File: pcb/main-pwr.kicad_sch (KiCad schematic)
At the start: 22 parts, among them U2 ADP5054

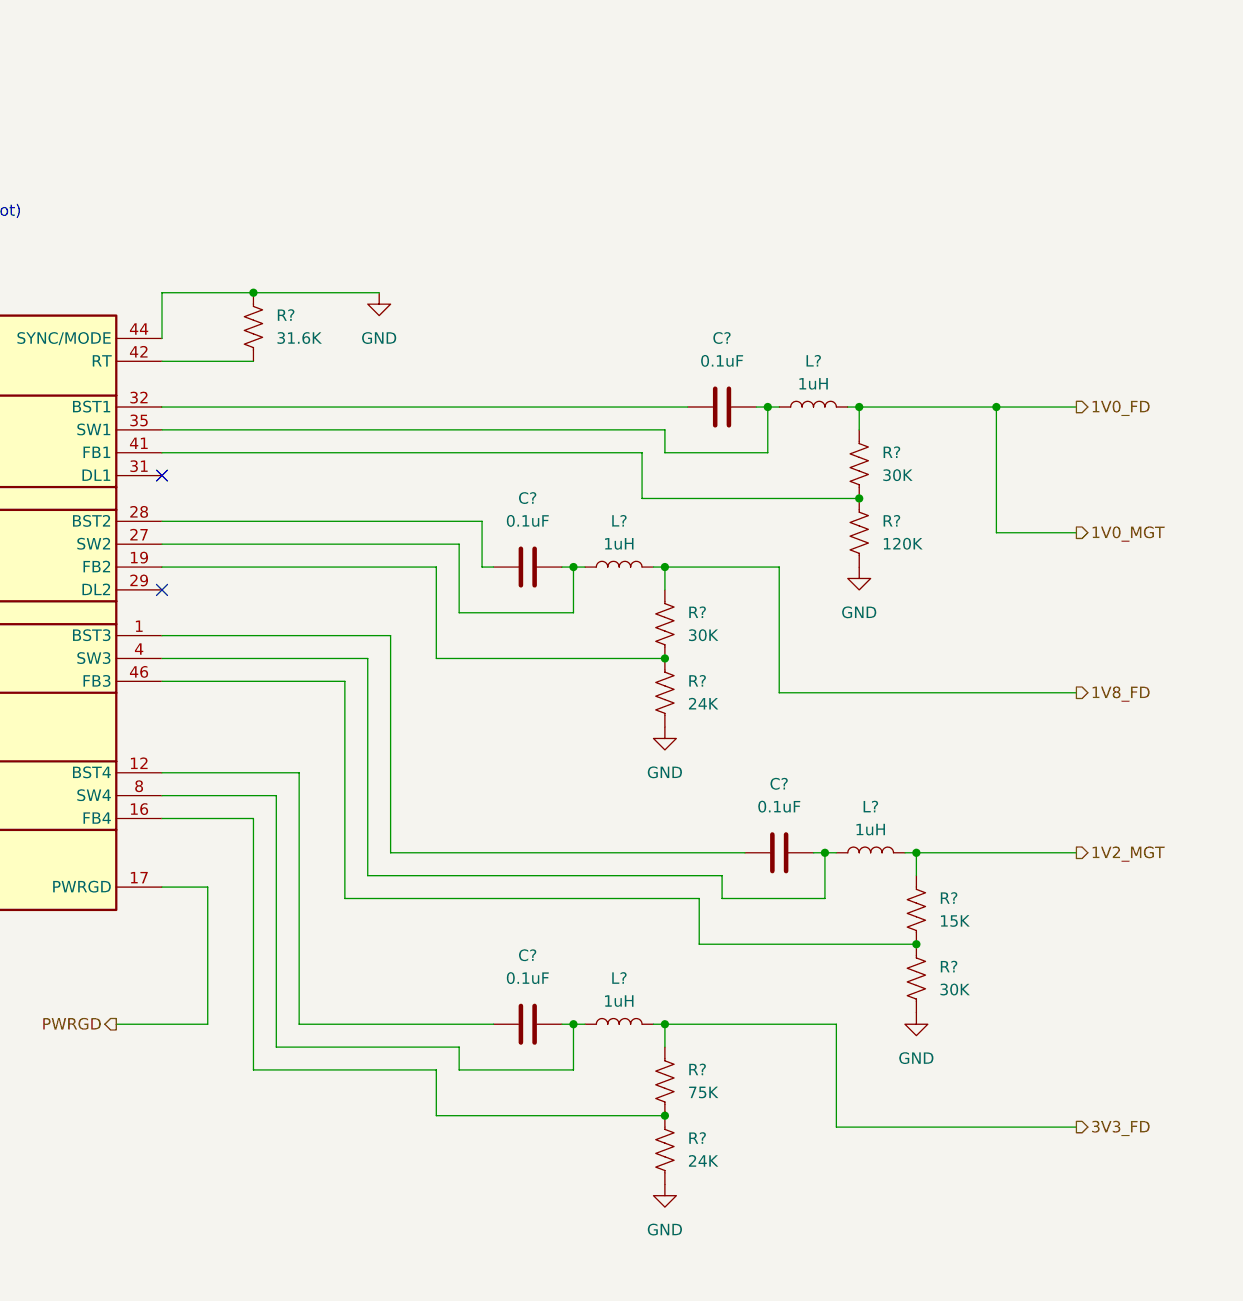
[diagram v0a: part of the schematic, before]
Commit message: current sense hierarchy definition
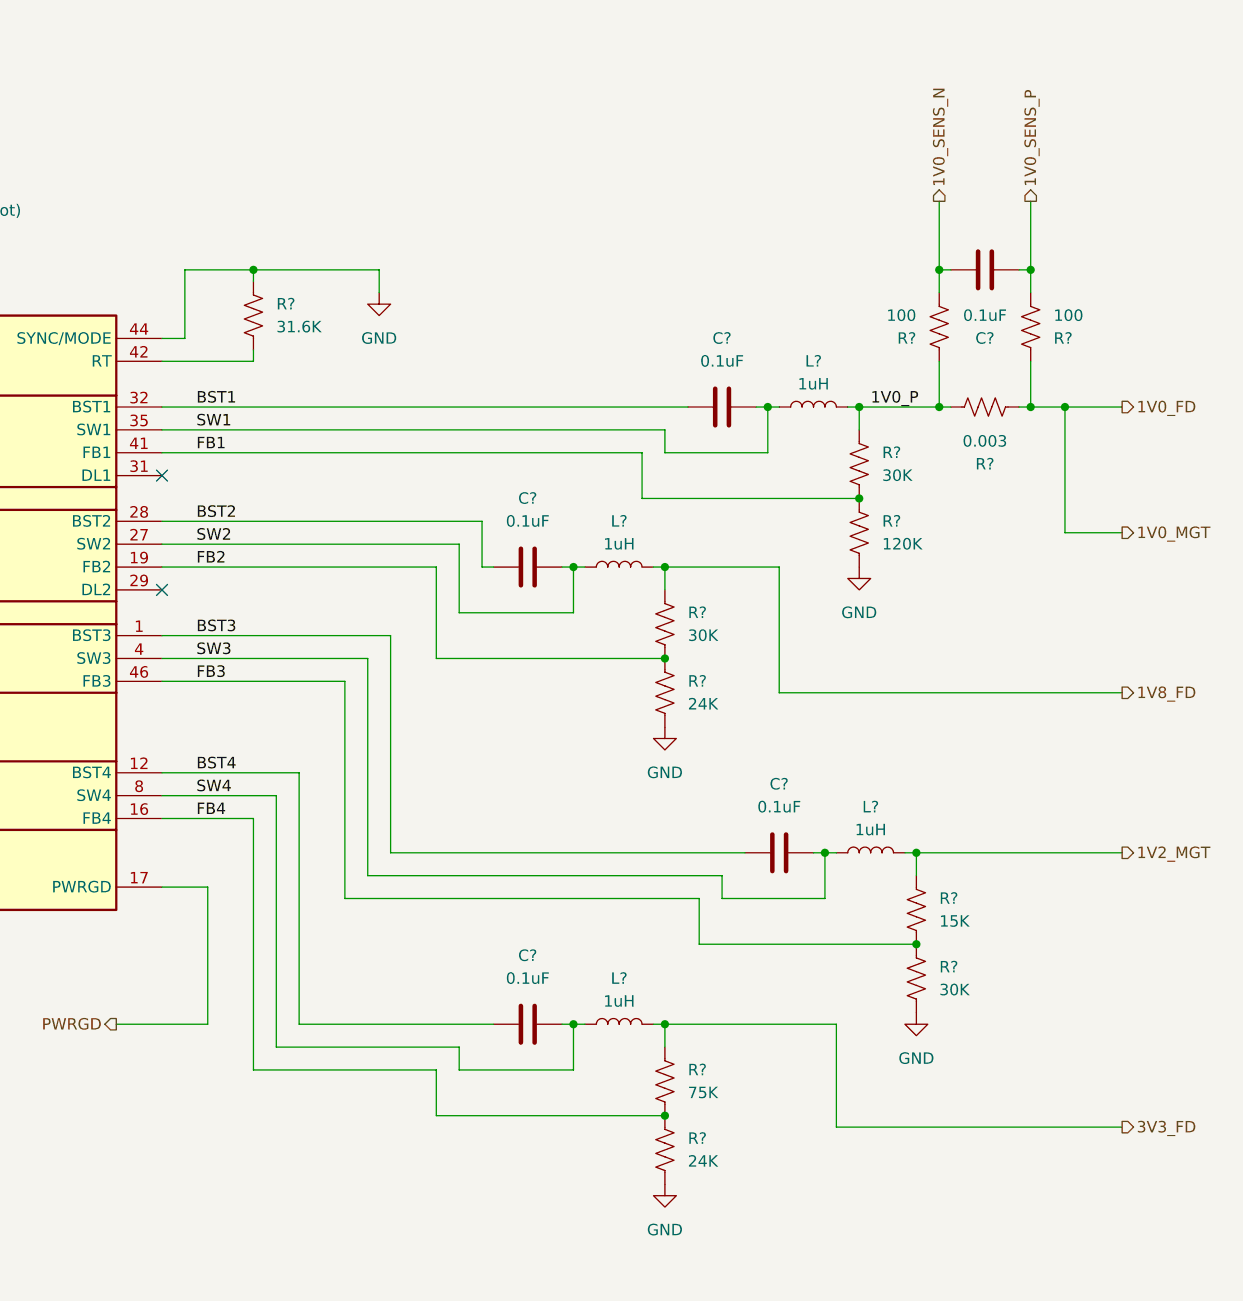
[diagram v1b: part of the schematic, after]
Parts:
- added C?: 0.1uF, symbol Device:C
- added R?: 0.003, symbol Device:R_US
- added R? (x2): 100, symbol Device:R_US
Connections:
- net 1V0_FD: now also R?.1, R?.2; no longer L?.2, R?.1
- net FB1: now reaches R?.1, R?.2, U2.33 (SW1), U2.34 (SW1), U2.41 (FB1)
- net FB3: now reaches R?.1, R?.2, U2.46 (FB3)
- net SW4: now reaches C?.2, L?.1, U2.8 (SW4), U2.9 (SW4)
- net BST3: now reaches C?.1, U2.1 (BST3)
- net BST4: now reaches C?.1, U2.12 (BST4)
- net FB4: now reaches R?.1, R?.2, U2.16 (FB4)
- net FB2: now reaches R?.1, R?.2, U2.19 (FB2)
- net SW2: now reaches C?.2, L?.1, U2.25 (SW2), U2.26 (SW2), U2.27 (SW2)
- net BST2: now reaches C?.1, U2.28 (BST2)
- net BST1: now reaches C?.1, U2.32 (BST1)
- net SW1: now reaches C?.2, L?.1, U2.35 (SW1)
- net SW3: now reaches C?.2, L?.1, U2.4 (SW3), U2.5 (SW3)
- new net 1V0_P: L?.2, R?.1, R?.2, R?.2
- new net 1V0_SENS_N: C?.2, R?.1
- new net 1V0_SENS_P: C?.1, R?.1
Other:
- moved on the sheet: R?

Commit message: changed spi flash to wson
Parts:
- C10, C11, C6, C7, C8, C9: renamed from C?; footprint (none) -> Capacitor_SMD:C_0402_1005Metric
- L1, L2, L3, L4: renamed from L?; footprint (none) -> Inductor_SMD:L_0402_1005Metric
- R10, R11, R12, R13, R14, R15, R16, R17, R19, R5, R7, R8, R9: renamed from R?; footprint (none) -> Resistor_SMD:R_0402_1005Metric
- R18: renamed from R?; value 0.003 -> 0.005; footprint (none) -> Resistor_SMD:R_0603_1608Metric
- R6: renamed from R?; footprint (none) -> Resistor_SMD:R_0805_2012Metric

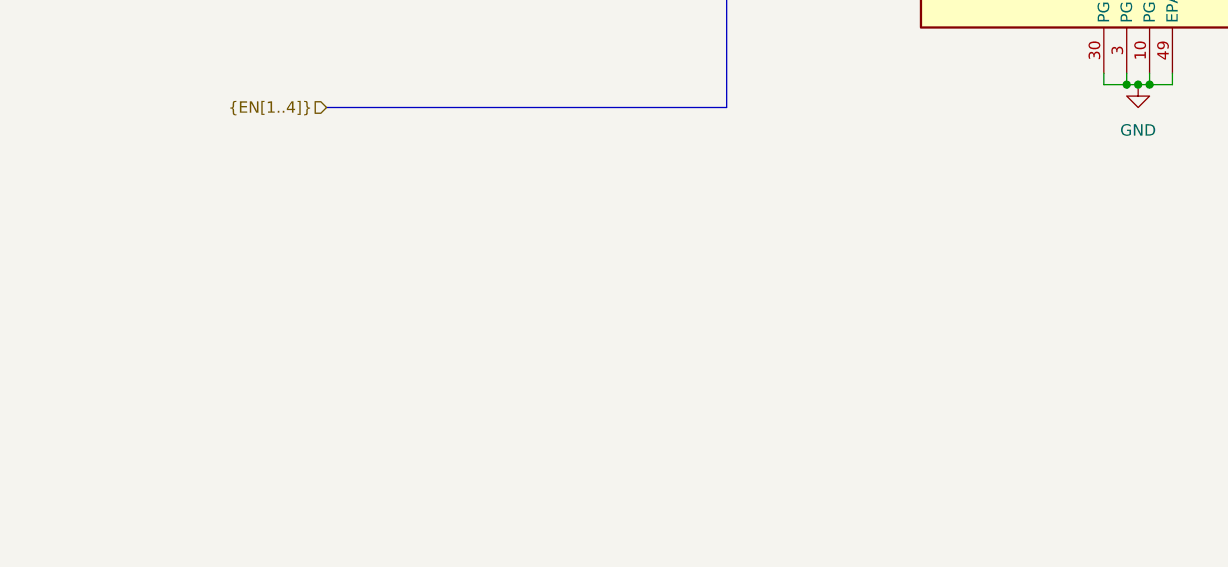
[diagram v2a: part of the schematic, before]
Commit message: added potential power sequencer
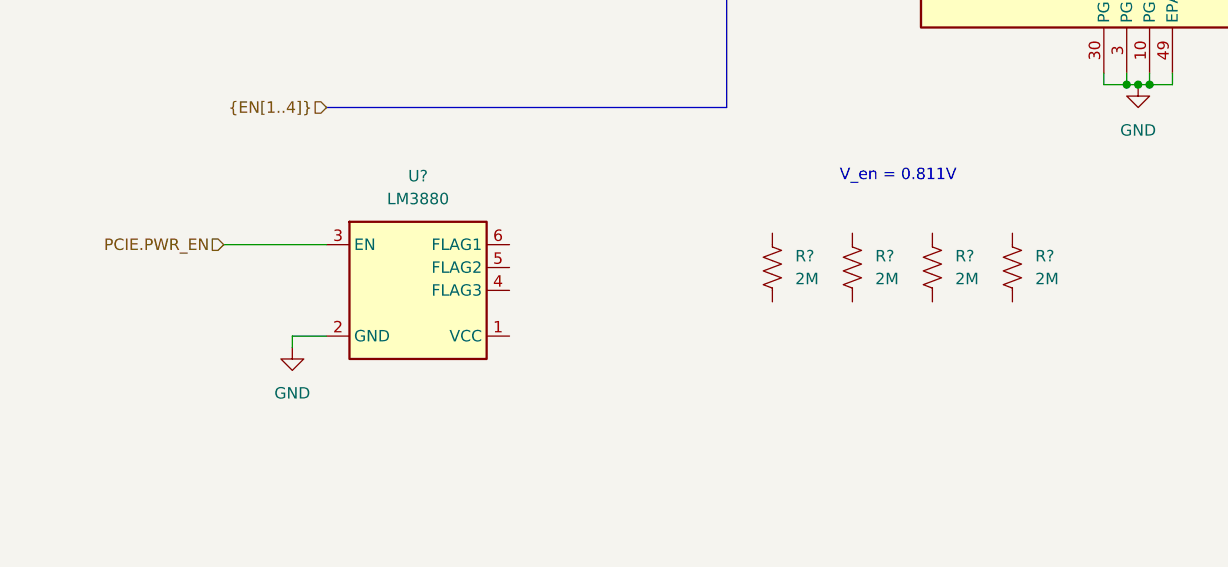
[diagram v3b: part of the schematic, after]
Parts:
- added R? (x4): 2M, symbol Device:R_US
- added U?: LM3880, Package_TO_SOT_SMD:SOT-23-6, symbol Power_Supervisor:LM3880
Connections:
- net GND: now also U?.2 (GND)
- new net PCIE.PWR_EN: U?.3 (EN)
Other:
- note added: "V_en = 0.811V"

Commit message: saved libraries to project
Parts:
- C10, C11, C6, C7, C8, C9: symbol Device:C -> library:C
- L1, L2, L3, L4: symbol Device:L -> library:L
- R10, R11, R12, R13, R14, R15, R16, R17, R18, R19, R5, R6, R7, R8, R9, R? (x4): symbol Device:R_US -> library:R_US
- U2: symbol Regulator_Switching:ADP5054 -> library:ADP5054
- U?: symbol Power_Supervisor:LM3880 -> library:LM3880
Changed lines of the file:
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@@
 	)
 	(symbol
-		(lib_id "Device:R_US")
+		(lib_id "library:R_US")
 		(at 243.84 76.2 0)
 		(unit 1)
@@
 	)
 	(symbol
-		(lib_id "Device:R_US")
+		(lib_id "library:R_US")
 		(at 257.81 62.23 270)
 		(unit 1)
@@
 	)
 	(symbol
-		(lib_id "Device:R_US")
+		(lib_id "library:R_US")
 		(at 250.19 125.73 0)
 		(unit 1)
@@
 	)
 	(symbol
-		(lib_id "Device:C")
+		(lib_id "library:C")
 		(at 257.81 46.99 270)
 		(unit 1)
@@
 	)
 	(symbol
-		(lib_id "Device:L")
+		(lib_id "library:L")
 		(at 217.17 130.81 90)
 		(unit 1)
@@
 	)
 	(symbol
-		(lib_id "Regulator_Switching:ADP5054")
+		(lib_id "library:ADP5054")
 		(at 138.43 74.93 0)
 		(unit 1)
@@
 	)
 	(symbol
-		(lib_id "power:GND")
+		(lib_id "library:GND")
 		(at 45.72 153.67 0)
 		(unit 1)
@@
 	)
 	(symbol
-		(lib_id "power:GND")
+		(lib_id "library:GND")
 		(at 250.19 129.54 0)
 		(unit 1)
@@
 	)
 	(symbol
-		(lib_id "Device:R_US")
+		(lib_id "library:R_US")
 		(at 222.25 86.36 0)
 		(unit 1)
@@
 	)
 	(symbol
-		(lib_id "Device:R_US")
+		(lib_id "library:R_US")
 		(at 250.19 118.11 0)
 		(unit 1)
@@
 	)
 	(symbol
-		(lib_id "Device:R_US")
+		(lib_id "library:R_US")
 		(at 107.95 144.78 0)
 		(unit 1)
@@
 	)
 	(symbol
-		(lib_id "Device:R_US")
+		(lib_id "library:R_US")
 		(at 176.53 52.07 0)
 		(unit 1)
@@
 	)
 	(symbol
-		(lib_id "Device:R_US")
+		(lib_id "library:R_US")
 		(at 222.25 93.98 0)
 		(unit 1)
@@
 	)
 	(symbol
-		(lib_id "Device:C")
+		(lib_id "library:C")
 		(at 207.01 80.01 90)
 		(unit 1)
@@
 	)
 	(symbol
-		(lib_id "power:GND")
+		(lib_id "library:GND")
 		(at 222.25 148.59 0)
 		(unit 1)
@@
 	)
 	(symbol
-		(lib_id "Device:R_US")
+		(lib_id "library:R_US")
 		(at 222.25 144.78 0)
 		(unit 1)
@@
 	)
 	(symbol
-		(lib_id "Device:L")
+		(lib_id "library:L")
 		(at 245.11 111.76 90)
 		(unit 1)
@@
 	)
 	(symbol
-		(lib_id "Device:R_US")
+		(lib_id "library:R_US")
 		(at 99.06 144.78 0)
 		(unit 1)
@@
 	)
 	(symbol
-		(lib_id "Device:L")
+		(lib_id "library:L")
 		(at 238.76 62.23 90)
 		(unit 1)
@@
 	)
 	(symbol
-		(lib_id "power:GND")
+		(lib_id "library:GND")
 		(at 222.25 97.79 0)
 		(unit 1)
@@
 	)
 	(symbol
-		(lib_id "Device:R_US")
+		(lib_id "library:R_US")
 		(at 125.73 144.78 0)
 		(unit 1)
@@
 	)
 	(symbol
-		(lib_id "Device:R_US")
+		(lib_id "library:R_US")
 		(at 222.25 137.16 0)
 		(unit 1)
@@
 	)
 	(symbol
-		(lib_id "Device:L")
+		(lib_id "library:L")
 		(at 217.17 80.01 90)
 		(unit 1)
@@
 	)
 	(symbol
-		(lib_id "Device:R_US")
+		(lib_id "library:R_US")
 		(at 36.83 26.67 90)
 		(unit 1)
@@
 	)
 	(symbol
-		(lib_id "Device:R_US")
+		(lib_id "library:R_US")
 		(at 45.72 35.56 180)
 		(unit 1)
@@
 	)
 	(symbol
-		(lib_id "Device:C")
+		(lib_id "library:C")
 		(at 234.95 111.76 90)
 		(unit 1)
@@
 	)
 	(symbol
-		(lib_id "Device:R_US")
+		(lib_id "library:R_US")
 		(at 27.94 35.56 180)
 		(unit 1)
@@
 	)
 	(symbol
-		(lib_id "Device:R_US")
+		(lib_id "library:R_US")
 		(at 262.89 53.34 0)
 		(unit 1)
@@
 	)
 	(symbol
-		(lib_id "Device:C")
+		(lib_id "library:C")
 		(at 36.83 41.91 90)
 		(unit 1)
@@
 	)
 	(symbol
-		(lib_id "power:GND")
+		(lib_id "library:GND")
 		(at 139.7 124.46 0)
 		(unit 1)
@@
 	)
 	(symbol
-		(lib_id "Power_Supervisor:LM3880")
+		(lib_id "library:LM3880")
 		(at 59.69 147.32 0)
 		(unit 1)
@@
 	)
 	(symbol
-		(lib_id "Device:C")
+		(lib_id "library:C")
 		(at 228.6 62.23 90)
 		(unit 1)
@@
 	)
 	(symbol
-		(lib_id "power:GND")
+		(lib_id "library:GND")
 		(at 190.5 49.53 0)
 		(unit 1)
@@
 	)
 	(symbol
-		(lib_id "Device:R_US")
+		(lib_id "library:R_US")
 		(at 116.84 144.78 0)
 		(unit 1)
@@
 	)
 	(symbol
-		(lib_id "Device:C")
+		(lib_id "library:C")
 		(at 207.01 130.81 90)
 		(unit 1)
@@
 	)
 	(symbol
-		(lib_id "power:GND")
+		(lib_id "library:GND")
 		(at 243.84 80.01 0)
 		(unit 1)
@@
 	)
 	(symbol
-		(lib_id "Device:R_US")
+		(lib_id "library:R_US")
 		(at 243.84 68.58 0)
 		(unit 1)
@@
 	)
 	(symbol
-		(lib_id "Device:R_US")
+		(lib_id "library:R_US")
 		(at 252.73 53.34 0)
 		(unit 1)

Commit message: sequencing initial connections
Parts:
- removed R?: 2M, symbol library:R_US
- removed U?: LM3880, Package_TO_SOT_SMD:SOT-23-6, symbol library:LM3880
- added U9: LM3880, Package_TO_SOT_SMD:SOT-23-6, symbol library:LM3880
- R? (x3): value 2M -> 100K
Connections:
- net EN1 is gone; now on net PCIE.PWR_EN: U2.39 (EN1)
- net 5V0_N: now also R?.2, R?.2, R?.2, U9.1 (VCC)
- net EN2: now also R?.1, U9.6 (FLAG1)
- net EN3: now also R?.1, U9.5 (FLAG2)
- net EN4: now also R?.1, U9.4 (FLAG3)
- net GND: now also U9.2 (GND)
- net PCIE.PWR_EN: now also U9.3 (EN)
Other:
- moved on the sheet: R?
